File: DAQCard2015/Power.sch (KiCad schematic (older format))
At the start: 33 parts, among them CON1 BARREL_JACK, SW1 SPST, U19 CDBHD240-G, U20 LM1086, U21 APXS002A0X-SRZ, U22 APXS002A0X-SRZ, U23 APXS002A0X-SRZ

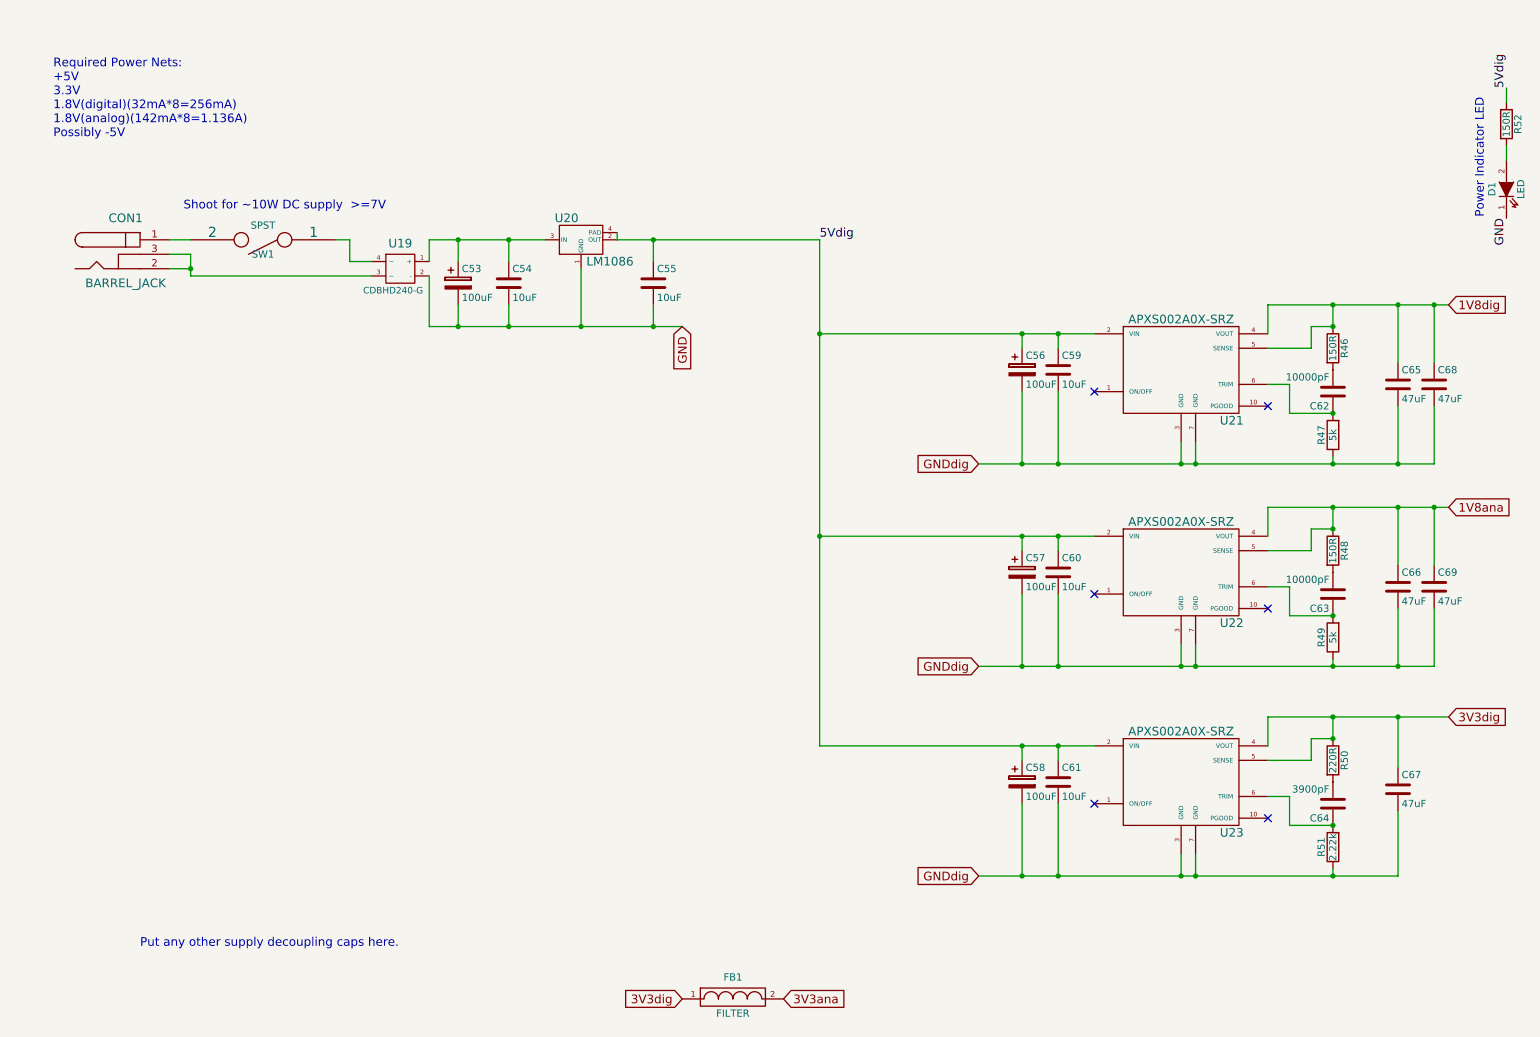
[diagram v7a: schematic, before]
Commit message: Updates to DAQ system including adjusting position of ZEM and adding Control signal outputs
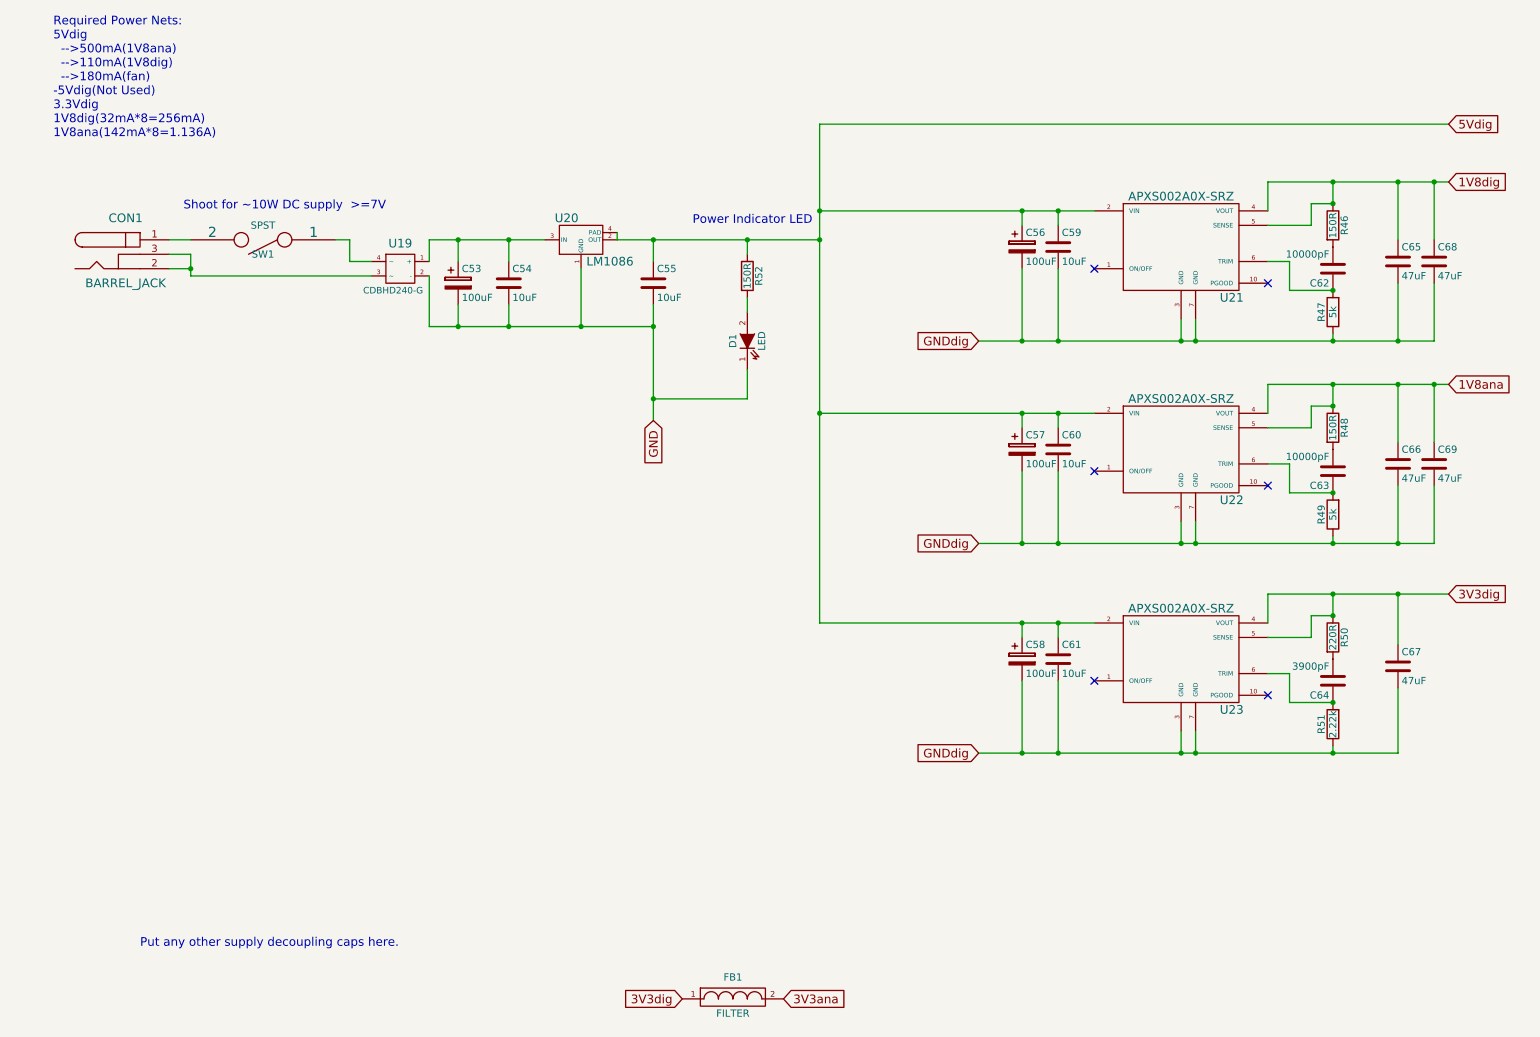
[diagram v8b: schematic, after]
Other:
- note added: "Required Power Nets:\n5Vdig\n -->500mA(1V8ana)\n -->110mA(1V8dig)\n -->180mA(fan)\n-5Vdig(Not Used)\n3.3Vdig\n1V8dig(32mA*8=256mA)\n1V8ana(142mA*8=1.136A)"
- note removed: "Required Power Nets:\n+5V\n3.3V\n1.8V(digital)(32mA*8=256mA)\n1.8V(analog)(142mA*8=1.136A)\nPossibly -5V"
- moved on the sheet: C56, C57, C58, C59, C60, C61, C62, C63, C64, C65, C66, C67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
